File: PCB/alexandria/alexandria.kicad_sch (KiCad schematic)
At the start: 6 parts, among them J1 AudioJack4, U1 ESP32-S3, U2 DFR0299, U3 TP4056-42-ESOP8, U4 CR2013-MI2120

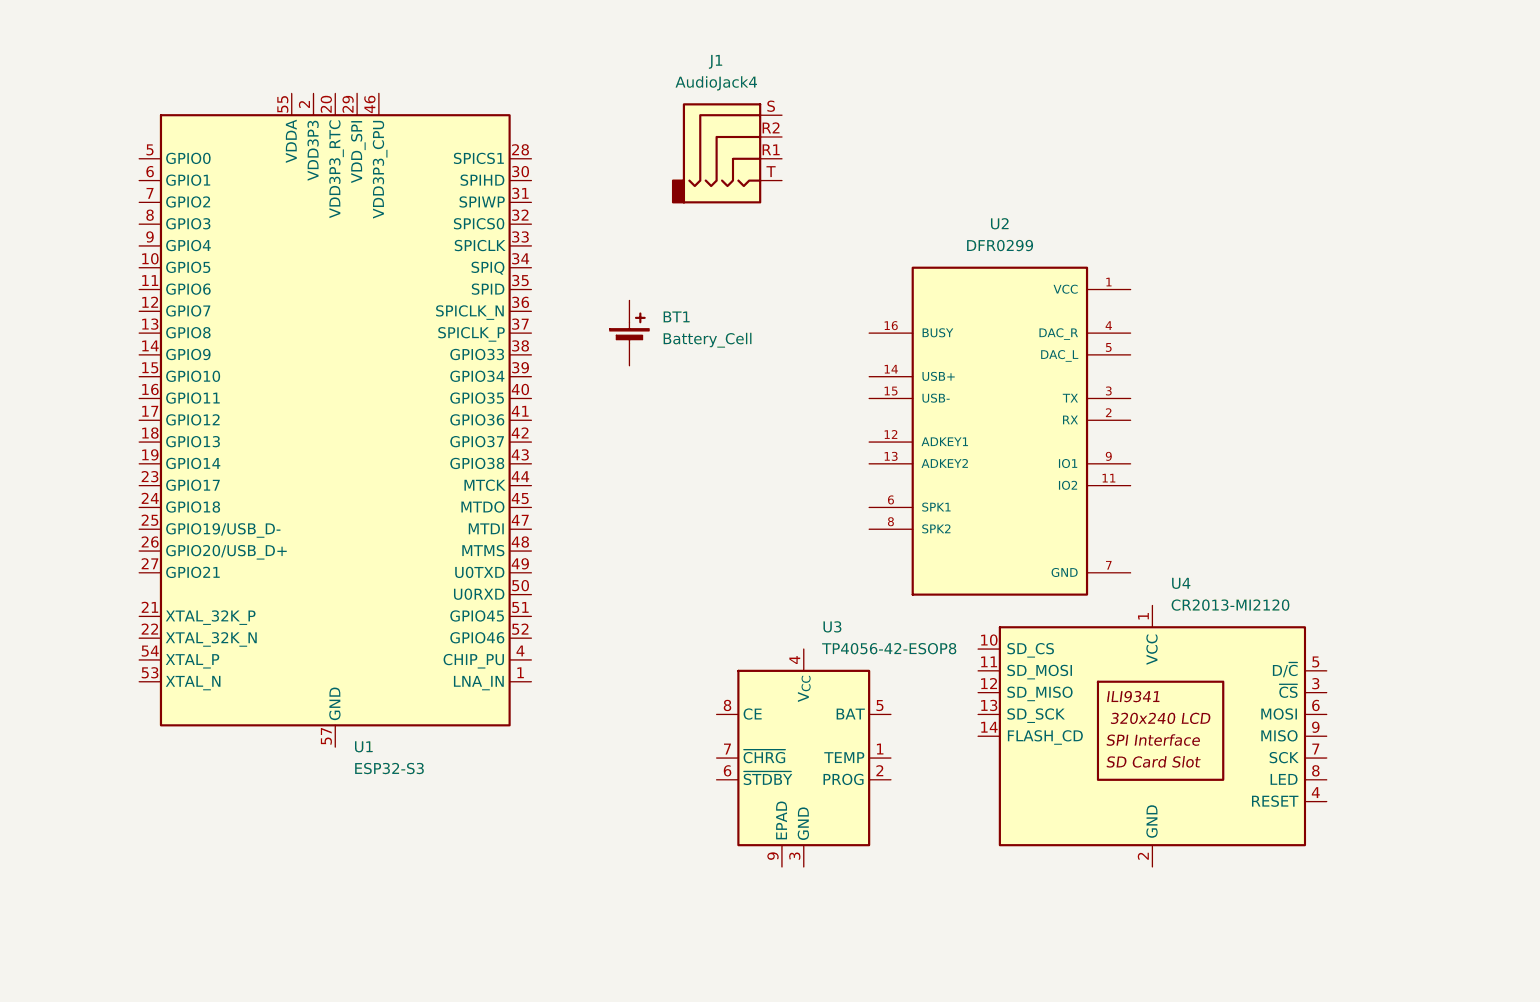
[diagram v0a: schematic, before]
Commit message: Add a power regulator and its do all the wiring for the schematic kicad file
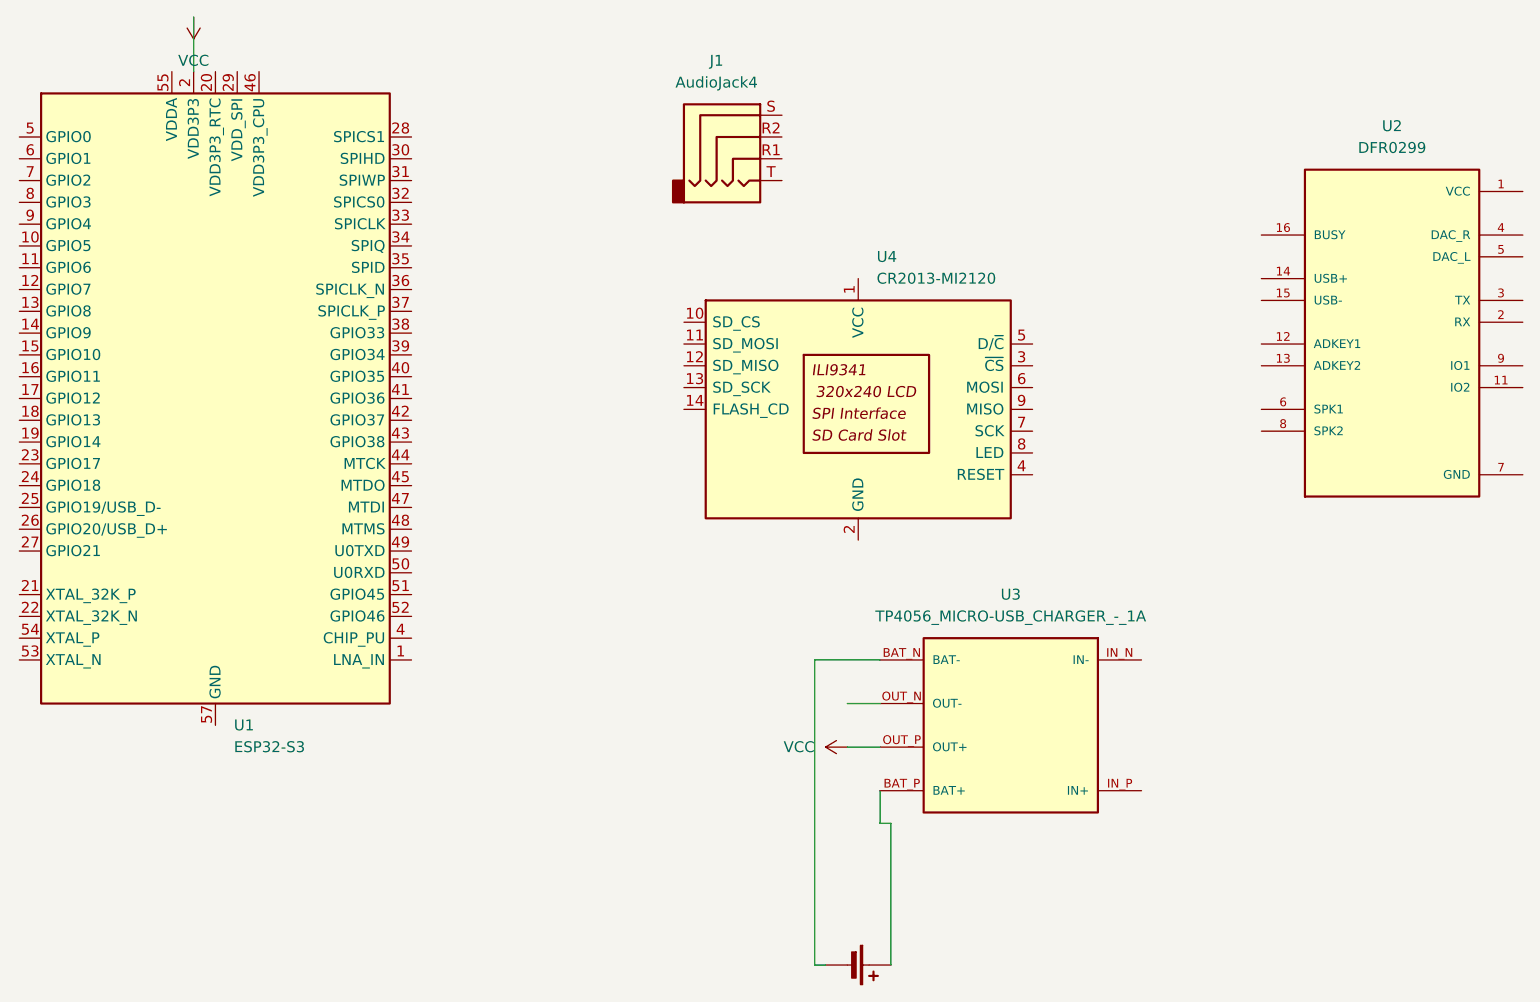
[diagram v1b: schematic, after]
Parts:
- removed U3: TP4056-42-ESOP8, Package_SO:SOIC-8-1EP_3.9x4.9mm_P1.27mm_EP2.41x3.3mm_ThermalVias, symbol Battery_Management:TP4056-42-ESOP8
- added U3: TP4056_MICRO-USB_CHARGER_-_1A, TP4056_MICRO-USB_CHARGER_-_1A:MODULE_TP4056_MICRO-USB_CHARGER_-_1A, symbol Kicad:TP4056_MICRO-USB_CHARGER_-_1A
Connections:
- net VCC: now reaches U1.2 (VDD3P3), U1.3 (VDD3P3)
- net VCC: now also U3.OUT_P (OUT+)
- net at BT1.1 (+): now also U3.BAT_P (BAT+)
- net at BT1.2 (-): now also U3.BAT_N (BAT-)
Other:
- moved on the sheet: U1, U2, U4
